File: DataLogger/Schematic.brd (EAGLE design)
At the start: 100 x 80 mm, 33 parts, among them IC1 MEGA8-AI, J1 DCJ0202, Q1 IRLML5203

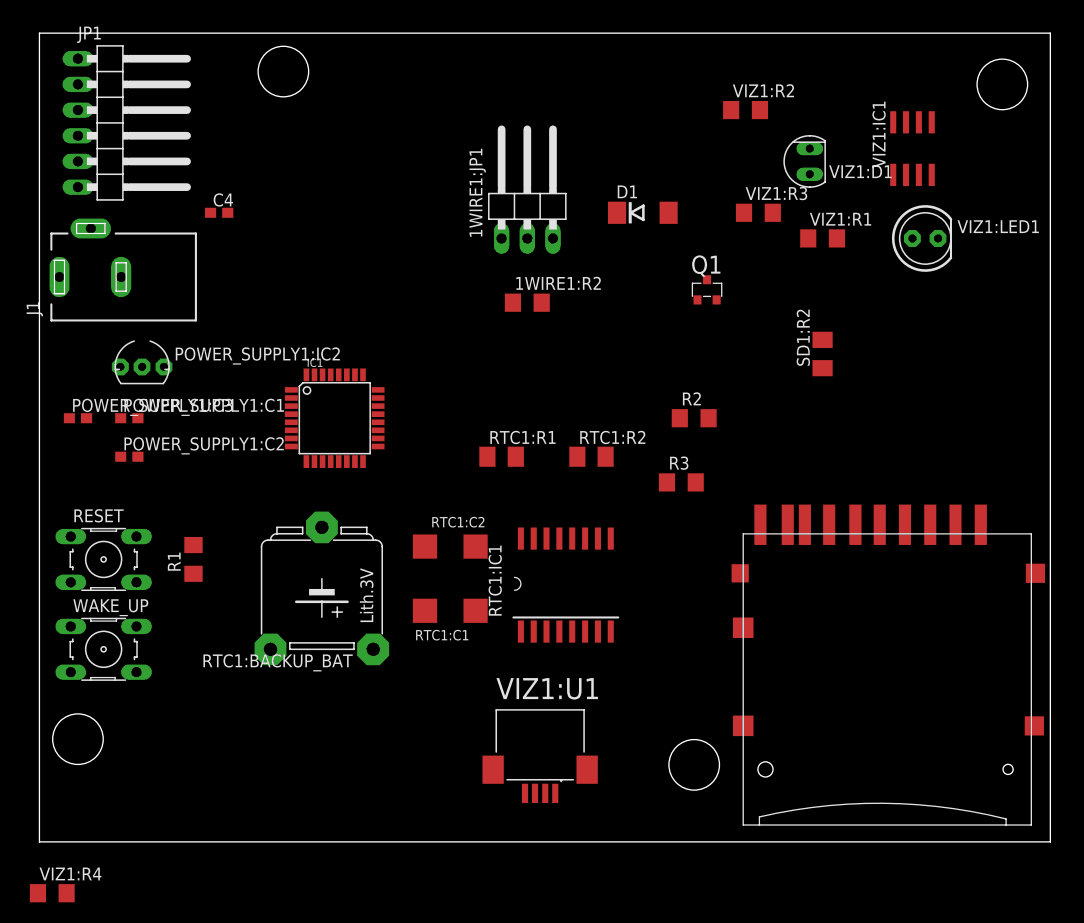
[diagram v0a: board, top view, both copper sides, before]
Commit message: Updated layout
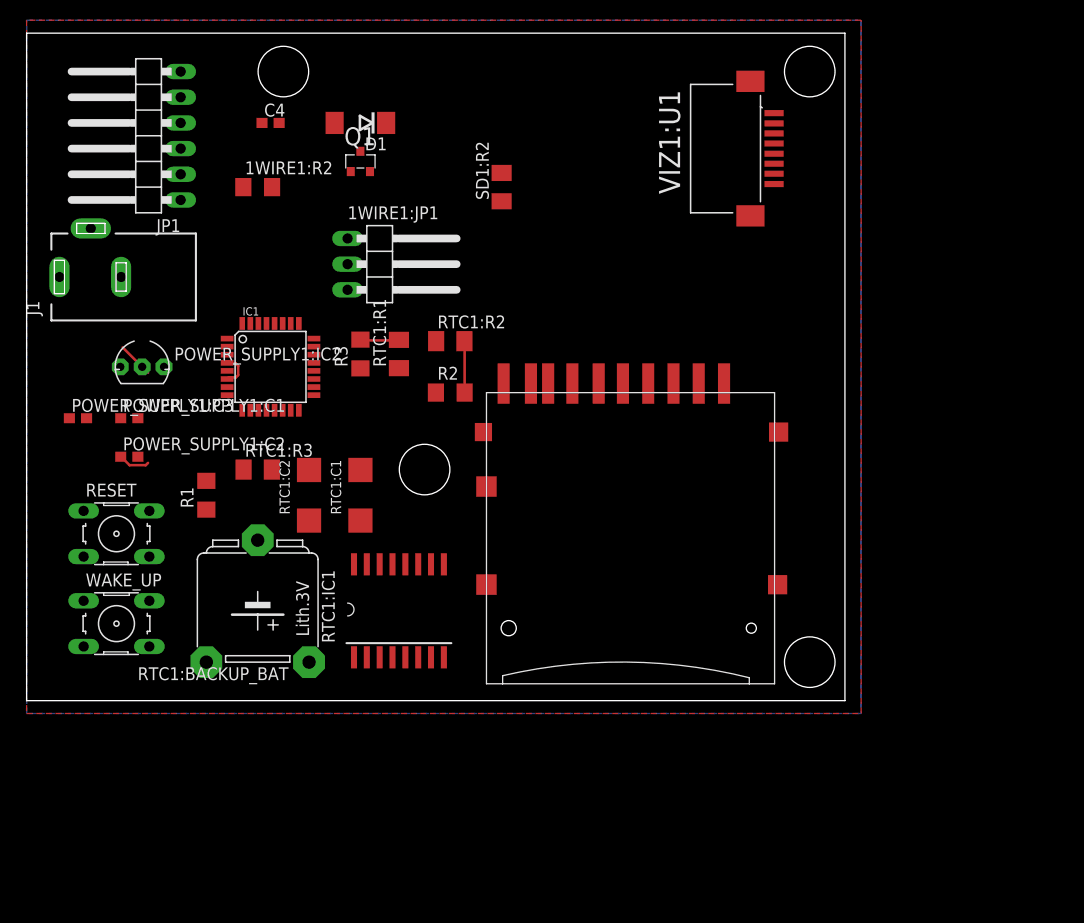
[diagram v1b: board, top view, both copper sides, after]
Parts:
- removed VIZ1:D1: SFH206, opto-trans-siemens:SFH206
- removed VIZ1:IC1: LM358D, linear:SO08
- removed VIZ1:LED1: (no value), adafruit:LED5MM
- removed VIZ1:R1: 1M, rcl:R1206
- removed VIZ1:R2: 22k, rcl:R1206
- removed VIZ1:R3: 180k, rcl:R1206
- removed VIZ1:R4: (no value), rcl:R1206
- added RTC1:R3: 10k, resistor:M1206
- RTC1:C1, RTC1:C2: value (none) -> 0.1F
- RTC1:IC1: value (none) -> DS3231SN
- RTC1:R1, RTC1:R2: value (none) -> 10k
- VIZ1:U1: value 52207-0485 -> 52207-0885; device Molex_By_element14_Batch_1:MOLEX_52207-0485 -> Molex_By_element14_Batch_1:MOLEX_52207-0885
- moved VIZ1:U1 74.1 mm to (77.5, 68.6), turned to 90 degrees
- moved Q1 36.6 mm to (31.8, 67.3)
- moved SD1:R2 35.8 mm to (45.7, 64.8)
- moved R3 34.2 mm to (31.8, 48.3), turned to 90 degrees
- moved D1 29.3 mm to (31.8, 71.1), turned to 180 degrees
- moved 1WIRE1:R2 29.0 mm to (21.6, 64.8)
- moved SD1:U$1 29.0 mm to (58.4, 44.5)
- moved R2 24.3 mm to (40.6, 44.5)
- moved RTC1:R2 18.1 mm to (40.6, 49.5)
- moved RTC1:IC1 16.7 mm to (35.6, 22.9)
- moved 1WIRE1:JP1 15.3 mm to (34.3, 57.1), turned to 270 degrees
- moved RTC1:C2 14.9 mm to (26.7, 34.3), turned to 90 degrees
- moved RTC1:C1 14.5 mm to (31.8, 34.3), turned to 90 degrees
- moved RTC1:R1 14.4 mm to (35.6, 48.3), turned to 90 degrees
- moved C4 10.2 mm to (22.9, 71.1)
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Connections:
- net N$12 renamed MOSI
- net N$14 renamed CS
- removed net N$11: IC1.16
- removed net N$13: IC1.17
- removed net N$19: IC1.24, VIZ1:IC1.1, VIZ1:R3.2
- removed net N$7: POWER_SUPPLY1:C1.2, POWER_SUPPLY1:C2.2, POWER_SUPPLY1:C3.2, POWER_SUPPLY1:IC2.1
- removed net RTC1:N$1: RTC1:IC1.15, RTC1:R2.1
- removed net RTC1:N$2: RTC1:IC1.16, RTC1:R1.1
- removed net SD1:MISO: SD1:U$1.7
- removed net SD1:SCK: SD1:U$1.5
- removed net VIZ1:N$1: VIZ1:D1.K, VIZ1:IC1.2, VIZ1:R1.1
- removed net VIZ1:N$2: VIZ1:LED1.A, VIZ1:R4.1
- removed net VIZ1:N$3: VIZ1:IC1.3, VIZ1:R2.2, VIZ1:R3.1
- new net MISO: IC1.16, SD1:U$1.7
- new net N$3: IC1.23, VIZ1:U1.3
- new net N$4: IC1.24, VIZ1:U1.4
- new net N$5: IC1.25, VIZ1:U1.5
- new net N$6: IC1.26, VIZ1:U1.6
- new net N$8: IC1.19, VIZ1:U1.7
- new net SCK: IC1.17, SD1:U$1.5
- new net SD1:CD: SD1:U$1.CD
- net GND: now also IC1.21, POWER_SUPPLY1:C1.2, POWER_SUPPLY1:C2.2, POWER_SUPPLY1:C3.2, POWER_SUPPLY1:IC2.1, VIZ1:U1.10, VIZ1:U1.8, VIZ1:U1.9; no longer VIZ1:D1.A, VIZ1:IC1.4, VIZ1:LED1.K, VIZ1:R2.1, VIZ1:U1.4, VIZ1:U1.5, VIZ1:U1.6
- net N$10: now also RTC1:IC1.15, RTC1:R2.1; no longer RTC1:R2.2
- net N$18: now also IC1.22; no longer IC1.23, VIZ1:R4.2
- net N$9: now also RTC1:IC1.16, RTC1:R1.1; no longer RTC1:R1.2
- net RTC1:32KHZ: now also RTC1:R3.1
- net TX: now also IC1.30
- net VCC: now also IC1.18, IC1.4, IC1.6, RTC1:R1.2, RTC1:R2.2, RTC1:R3.2, VIZ1:U1.1; no longer VIZ1:IC1.8, VIZ1:R1.2
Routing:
- net N$2: track 0.00 -> 6.87 mm
- net N$10: track 0.00 -> 4.93 mm
- net N$9: track 0.00 -> 3.74 mm
- net VCC: track 0.00 -> 3.36 mm
- added copper zone on layer 1, net GND
- added copper zone on layer 16, net GND
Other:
- board size 100 x 80 mm -> 81 x 66 mm

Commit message: Rerouted stuff and replaced with better parts.
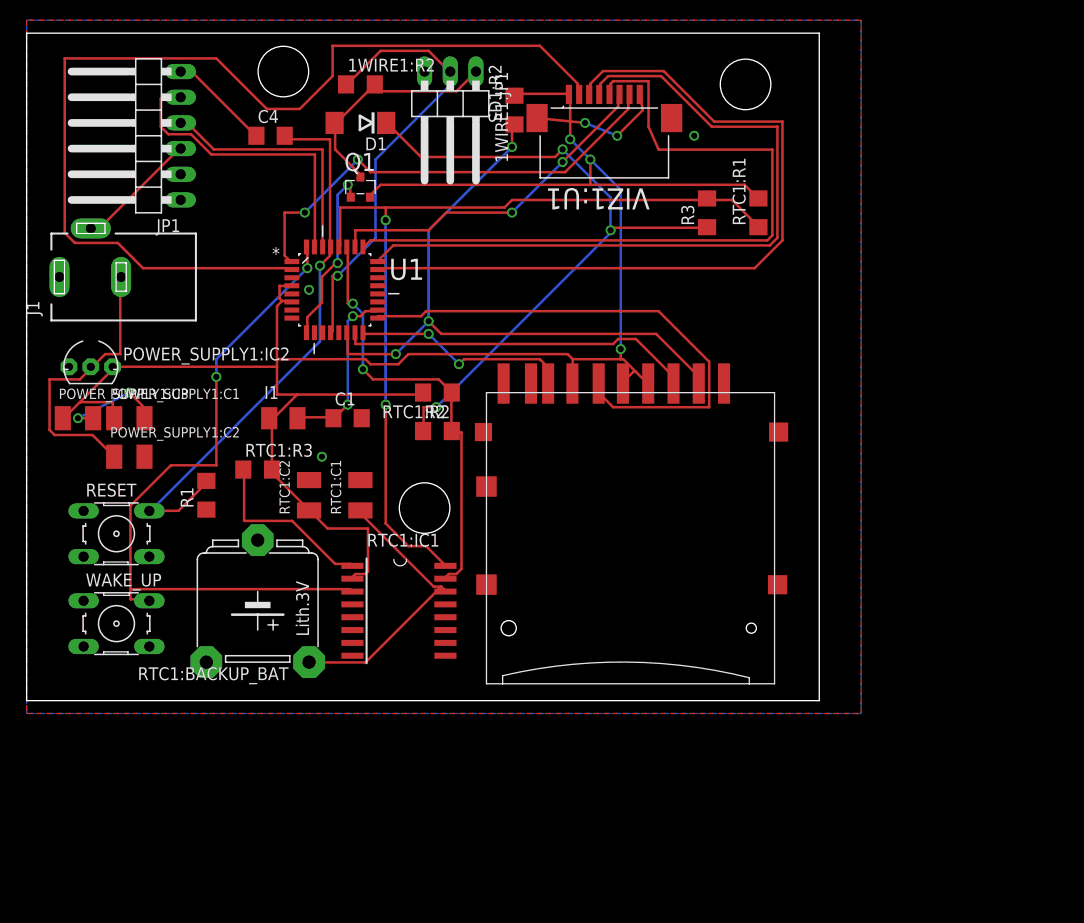
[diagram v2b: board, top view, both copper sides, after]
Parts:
- removed IC1: MEGA8-AI, avr-6:TQFP32-08
- added C1: 100nF, rcl:C1206
- added I1: 10nH, Element14Parts:L3225M
- added U1: ATMEGA328P-AU, atmel-atmeg328PU:QFP80P900X900X120-32N
- C4: device eagle-ltspice:C1608 -> rcl:C1206
- POWER_SUPPLY1:C1, POWER_SUPPLY1:C2, POWER_SUPPLY1:C3: device eagle-ltspice:C1608 -> rcl:SMC_B
- R1: device resistor:R1206 -> rcl:R1206
- RTC1:C1, RTC1:C2: device rcl:SMC_C -> rcl:SMC_B
- RTC1:R1, RTC1:R2, RTC1:R3: device resistor:M1206 -> rcl:R1206
- SD1:R2: device rcl:M1206 -> rcl:R1206
- moved RTC1:R1 38.2 mm to (71.1, 62.2)
- moved R3 37.0 mm to (66.0, 62.2)
- moved VIZ1:U1 23.9 mm to (55.9, 78.7), turned to 180 degrees
- moved 1WIRE1:JP1 16.5 mm to (40.6, 72.4), turned to 180 degrees
- moved 1WIRE1:R2 14.4 mm to (31.8, 74.9)
- moved SD1:R2 7.73 mm to (47.0, 72.4)
- moved RTC1:R2 5.24 mm to (39.4, 44.5), turned to 180 degrees
- moved POWER_SUPPLY1:IC2 5.08 mm to (5.08, 47.0)
- moved R2 4.02 mm to (39.4, 40.6)
- moved Q1 2.54 mm to (31.8, 64.8)
- moved C4 1.27 mm to (22.9, 69.8)
- turned RTC1:IC1 to 270 degrees
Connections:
- new net ADC6: U1.19
- new net ADC7: U1.22
- new net AREF: U1.20
- new net AVCC: C1.1, I1.2, U1.18
- net CS: now also U1.14; no longer IC1.14
- net GND: now also C1.2, POWER_SUPPLY1:C1.-, POWER_SUPPLY1:C2.-, POWER_SUPPLY1:C3.-, U1.21, U1.3, U1.5; no longer IC1.21, IC1.3, IC1.5, POWER_SUPPLY1:C1.2, POWER_SUPPLY1:C2.2, POWER_SUPPLY1:C3.2
- net MISO: now also U1.16; no longer IC1.16
- net MOSI: now also U1.15; no longer IC1.15
- net N$1: now also U1.9; no longer IC1.9
- net N$10: now also U1.27; no longer IC1.27
- net N$15: now also U1.32; no longer IC1.32
- net N$16: now also U1.12; no longer IC1.12
- net N$18: now also U1.2; no longer IC1.22
- net N$2: now also POWER_SUPPLY1:C2.+; no longer POWER_SUPPLY1:C2.1
- net N$3: now also U1.23; no longer IC1.23
- net N$4: now also U1.24; no longer IC1.24
- net N$5: now also U1.25; no longer IC1.25
- net N$6: now also U1.26; no longer IC1.26
- net N$8: now also U1.1; no longer IC1.19
- net N$9: now also U1.28; no longer IC1.28
- net RESET: now also U1.29; no longer IC1.29
- net RX: now also U1.31; no longer IC1.31
- net SCK: now also U1.17; no longer IC1.17
- net TX: now also U1.30; no longer IC1.30
- net VCC: now also I1.1, POWER_SUPPLY1:C1.+, POWER_SUPPLY1:C3.+, SD1:U$1.4, U1.4, U1.6; no longer IC1.18, IC1.4, IC1.6, POWER_SUPPLY1:C1.1, POWER_SUPPLY1:C3.1
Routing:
- net VCC: track 3.36 -> 202.4 mm, vias 0 -> 3
- net N$18: track 0.00 -> 101.1 mm
- net N$9: track 3.74 -> 85.8 mm, vias 0 -> 2
- net N$3: track 0.00 -> 75.8 mm
- net N$5: track 0.00 -> 72.6 mm
- net N$4: track 0.00 -> 72.6 mm
- net N$15: track 0.00 -> 68.8 mm, vias 0 -> 2
- net N$17: track 0.00 -> 67.0 mm, vias 0 -> 3
- net CS: track 0.00 -> 64.2 mm, vias 0 -> 3
- net RESET: track 0.00 -> 55.8 mm, vias 0 -> 1
- net SCK: track 0.00 -> 52.2 mm
- net N$8: track 0.00 -> 46.0 mm, vias 0 -> 2
- net N$16: track 0.00 -> 43.5 mm, vias 0 -> 1
- net N$10: track 4.93 -> 43.2 mm, vias 0 -> 2
- net MOSI: track 0.00 -> 35.1 mm
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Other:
- board size 81 x 66 mm -> 78.4 x 66 mm

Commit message: Improvements
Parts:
- added D2: (no value), diode:DO214AA
- U1: device atmel-atmeg328PU:QFP80P900X900X120-32N -> Arduino Dev Parts:TQFP32-08
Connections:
- net CS renamed D10
- net MISO renamed D12
- net MOSI renamed D11
- net N$1 renamed D5
- net N$10 renamed A4
- net N$15 renamed D2
- net N$16 renamed D8
- net N$18 renamed D4
- net N$3 renamed A0
- net N$4 renamed A1
- net N$5 renamed A2
- net N$6 renamed A3
- net N$8 renamed D3
- net N$9 renamed A5
- net SCK renamed D13
- removed net ADC6: U1.19
- removed net ADC7: U1.22
- new net N$1: D2.A, J1.3
- net N$2: now also D2.C; no longer J1.3
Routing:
- net GND: track 23.6 -> 351.4 mm, vias 7 -> 2
- net VCC: track 202.4 -> 280.6 mm, vias 3 -> 5
- net D4: track 101.1 -> 39.8 mm, vias 0 -> 2
- net D10: track 64.2 -> 115.2 mm, vias 3 -> 0
- net A1: track 72.6 -> 31.5 mm
- net A2: track 72.6 -> 33.4 mm, vias 0 -> 4
- net A0: track 75.8 -> 44.3 mm
- net D2: track 68.8 -> 99.8 mm, vias 2 -> 0
- net D13: track 52.2 -> 24.9 mm, vias 0 -> 2
- net A4: track 43.2 -> 64.3 mm, vias 2 -> 4
- net D12: track 21.7 -> 34.4 mm, vias 2 -> 0
- net N$2: track 28.2 -> 18.1 mm
- net N$1: track 0.00 -> 9.77 mm
- net D3: track 46.0 -> 54.7 mm
- net RESET: track 55.8 -> 48.0 mm, vias 1 -> 0
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- removed copper zone on layer 1, net GND
- removed copper zone on layer 16, net GND
